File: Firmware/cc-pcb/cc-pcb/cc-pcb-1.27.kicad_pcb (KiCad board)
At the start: 2 copper layers, 39.4 x 36.8 mm, 19 parts, among them CON1 BARREL_JACK, IC1 ATMEGA328P-A, P1 CONN_20, P4 CONN_2, P5 CONN_6, P6 CONN_6, SW1 SRS

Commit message: cleaning up
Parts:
- CON1: value BARREL_JACK -> (none)
- D1, D2, D3, D4, D5, D6: value DIODE -> (none)
- IC1: value ATMEGA328P-A -> (none)
- P1: value CONN_20 -> (none)
- P4: value CONN_2 -> (none)
- P5, P6: value CONN_6 -> (none)
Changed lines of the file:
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@@
     (visible_elements 7FFFFBFF)
     (pcbplotparams
-      (layerselection 3178497)
+      (layerselection 284196865)
       (usegerberextensions true)
       (excludeedgelayer true)
@@
       (outputformat 1)
       (mirror false)
-      (drillshape 1)
+      (drillshape 0)
       (scaleselection 1)
-      (outputdirectory ""))
+      (outputdirectory D:/Tests/workspace/4DMC-Model/Firmware/cc-pcb/cc-pcb/))
   )
   (net 0 "")
@@
       (effects (font (size 1.016 1.016) (thickness 0.2032)))
     )
-    (fp_text value CONN_6 (at 0 3.81 180) (layer F.SilkS) hide
+    (fp_text value "" (at 0 3.81 180) (layer F.SilkS) hide
       (effects (font (size 1.016 1.016) (thickness 0.2032)))
     )
@@
       (effects (font (size 1.016 1.016) (thickness 0.2032)))
     )
-    (fp_text value CONN_6 (at 0 2.159 270) (layer F.SilkS) hide
+    (fp_text value "" (at 0 2.159 270) (layer F.SilkS) hide
       (effects (font (size 1.016 0.889) (thickness 0.2032)))
     )
@@
     (at 189.992 75.184)
     (descr "Hole 2mm")
-    (fp_text reference H1 (at 0 -2.794) (layer F.SilkS)
+    (fp_text reference H1 (at 0 -2.794) (layer F.SilkS) hide
       (effects (font (size 1.524 1.524) (thickness 0.3048)))
     )
@@
     (at 189.992 106.172)
     (descr "Hole 2mm")
-    (fp_text reference H2 (at 0 -2.794) (layer F.SilkS)
+    (fp_text reference H2 (at 0 -2.794) (layer F.SilkS) hide
       (effects (font (size 1.524 1.524) (thickness 0.3048)))
     )
@@
     (at 156.972 106.172)
     (descr "Hole 2mm")
-    (fp_text reference H3 (at 0 -2.794) (layer F.SilkS)
+    (fp_text reference H3 (at 0 -2.794) (layer F.SilkS) hide
       (effects (font (size 1.524 1.524) (thickness 0.3048)))
     )
@@
       (effects (font (size 1 1) (thickness 0.15)))
     )
-    (fp_text value CONN_20 (at 0 -3.8 90) (layer F.SilkS) hide
+    (fp_text value "" (at 0 -3.8 90) (layer F.SilkS) hide
       (effects (font (size 1 1) (thickness 0.15)))
     )
@@
   (module TQFP32 (layer F.Cu)
     (at 168.402 92.456 270)
-    (fp_text reference IC1 (at 0 -1.27 270) (layer F.SilkS)
+    (fp_text reference IC1 (at 0 0 270) (layer F.SilkS)
       (effects (font (size 1.27 1.016) (thickness 0.2032)))
     )
-    (fp_text value ATMEGA328P-A (at 0 1.905 270) (layer F.SilkS)
+    (fp_text value "" (at 0 1.905 270) (layer F.SilkS)
       (effects (font (size 1.27 1.016) (thickness 0.2032)))
     )
@@
       (effects (font (size 0.39878 0.39878) (thickness 0.09906)))
     )
-    (fp_text value DIODE (at 0 1.19888 90) (layer F.SilkS) hide
+    (fp_text value "" (at 0 1.19888 90) (layer F.SilkS) hide
       (effects (font (size 0.39878 0.39878) (thickness 0.09906)))
     )
@@
       (effects (font (size 0.39878 0.39878) (thickness 0.09906)))
     )
-    (fp_text value DIODE (at 0 1.19888 90) (layer F.SilkS) hide
+    (fp_text value "" (at 0 1.19888 90) (layer F.SilkS) hide
       (effects (font (size 0.39878 0.39878) (thickness 0.09906)))
     )
@@
       (effects (font (size 0.39878 0.39878) (thickness 0.09906)))
     )
-    (fp_text value DIODE (at 0 1.19888 90) (layer F.SilkS) hide
+    (fp_text value "" (at 0 1.19888 90) (layer F.SilkS) hide
       (effects (font (size 0.39878 0.39878) (thickness 0.09906)))
     )
@@
       (effects (font (size 0.39878 0.39878) (thickness 0.09906)))
     )
-    (fp_text value DIODE (at 0 1.19888 180) (layer F.SilkS) hide
+    (fp_text value "" (at 0 1.19888 180) (layer F.SilkS) hide
       (effects (font (size 0.39878 0.39878) (thickness 0.09906)))
     )
@@
       (effects (font (size 0.39878 0.39878) (thickness 0.09906)))
     )
-    (fp_text value DIODE (at 0 1.19888 180) (layer F.SilkS) hide
+    (fp_text value "" (at 0 1.19888 180) (layer F.SilkS) hide
       (effects (font (size 0.39878 0.39878) (thickness 0.09906)))
     )
@@
       (effects (font (size 0.39878 0.39878) (thickness 0.09906)))
     )
-    (fp_text value DIODE (at 0 1.19888 180) (layer F.SilkS) hide
+    (fp_text value "" (at 0 1.19888 180) (layer F.SilkS) hide
       (effects (font (size 0.39878 0.39878) (thickness 0.09906)))
     )
@@
       (effects (font (size 1.016 1.016) (thickness 0.2032)))
     )
-    (fp_text value CONN_2 (at 0.254 -3.556 90) (layer F.SilkS) hide
+    (fp_text value "" (at 0.254 -3.556 90) (layer F.SilkS) hide
       (effects (font (size 1.016 0.889) (thickness 0.2032)))
     )
@@
     (descr "DC Barrel Jack")
     (tags "Power Jack")
-    (fp_text reference CON1 (at 10.09904 0 90) (layer F.SilkS)
+    (fp_text reference CON1 (at 10.09904 0 90) (layer F.SilkS) hide
       (effects (font (size 1.016 1.016) (thickness 0.2032)))
     )
-    (fp_text value BARREL_JACK (at 0 -5.99948) (layer F.SilkS) hide
+    (fp_text value "" (at 0 -5.99948) (layer F.SilkS) hide
       (effects (font (size 1.016 1.016) (thickness 0.2032)))
     )
@@
   (segment (start 167.894002 83.438998) (end 175.178302 83.438998) (width 0.254) (layer F.Cu) (net 30))
   (segment (start 163.6268 87.7062) (end 167.894002 83.438998) (width 0.254) (layer F.Cu) (net 30))
-  (segment (start 157.48 94.996) (end 156.464 94.996) (width 1.016) (layer B.Cu) (net 31) (status 400000))
+  (segment (start 157.48 94.996) (end 156.464 94.996) (width 1.016) (layer B.Cu) (net 31))
   (segment (start 156.464 94.996) (end 155.575 94.107) (width 1.016) (layer B.Cu) (net 31))
   (segment (start 155.575 94.107) (end 155.575 85.471) (width 1.016) (layer B.Cu) (net 31))
@@
     (polygon
       (pts
-        (xy 191.008 95.25) (xy 187.198 99.187) (xy 187.198 109.22) (xy 159.766 109.22) (xy 159.766 103.378)
+        (xy 191.008 95.377) (xy 187.198 99.187) (xy 187.198 109.093) (xy 159.766 109.22) (xy 159.766 103.378)
         (xy 153.67 103.378) (xy 153.67 72.39) (xy 187.198 72.39) (xy 187.198 77.851) (xy 191.008 81.661)
       )
@@
     (polygon
       (pts
-        (xy 191.008 92.583) (xy 187.198 96.393) (xy 187.198 109.22) (xy 159.766 109.22) (xy 159.766 103.378)
+        (xy 191.008 95.377) (xy 187.198 99.187) (xy 187.198 109.22) (xy 159.766 109.22) (xy 159.766 103.378)
         (xy 153.67 103.378) (xy 153.67 72.39) (xy 187.198 72.39) (xy 187.198 77.851) (xy 191.008 81.661)
       )
     )
+  )
+  (zone (net 0) (net_name "") (layer F.Cu) (hatch edge 0.508)
+    (connect_pads (clearance 0.508))
+    (min_thickness 0.254)
+    (keepout (tracks allowed) (vias allowed) (copperpour not_allowed))
+    (fill (arc_segments 16) (thermal_gap 0.508) (thermal_bridge_width 0.508))
+    (polygon
+      (pts
+        (xy 171.831 95.758) (xy 164.973 95.758) (xy 164.973 89.027) (xy 171.831 89.027)
+      )
+    )
+  )
+  (zone (net 0) (net_name "") (layer F.Cu) (hatch edge 0.508)
+    (connect_pads (clearance 0.508))
+    (min_thickness 0.254)
+    (keepout (tracks allowed) (vias allowed) (copperpour not_allowed))
+    (fill (arc_segments 16) (thermal_gap 0.508) (thermal_bridge_width 0.508))
+    (polygon
+      (pts
+        (xy 168.021 84.582) (xy 171.196 84.582) (xy 171.196 84.963) (xy 170.18 85.979) (xy 169.291 85.979)
+        (xy 168.529 85.344) (xy 167.259 85.344) (xy 168.021 84.582)
+      )
+    )

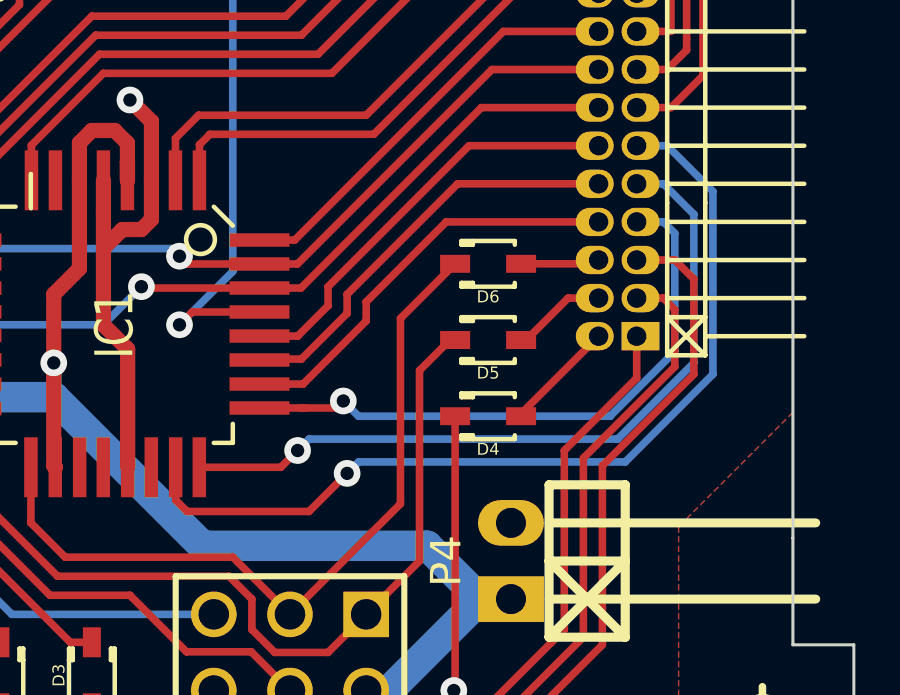
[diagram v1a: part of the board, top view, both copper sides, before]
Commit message: Increased GND width for LEDs
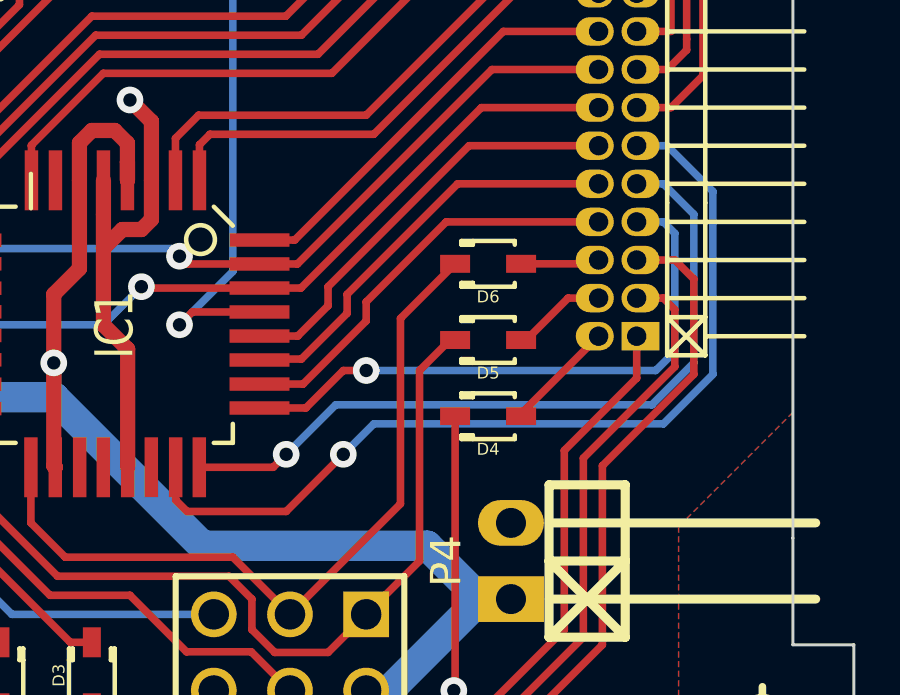
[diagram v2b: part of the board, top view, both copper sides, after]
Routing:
- net N-0000022: track 20.6 -> 20.0 mm
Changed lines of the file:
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@@
-(kicad_pcb (version 3) (host pcbnew "(2013-07-07 BZR 4022)-stable")
+(kicad_pcb (version 3) (host pcbnew "(2014-01-10 BZR 4027)-stable")
   (general
     (links 56)
@@
     (thickness 1.6)
     (drawings 9)
-    (tracks 309)
+    (tracks 306)
     (zones 0)
     (modules 19)
@@
     (19 F.Paste user)
     (20 B.SilkS user)
-    (21 F.SilkS user)
+    (21 F.SilkS user hide)
     (22 B.Mask user)
     (23 F.Mask user)
@@
   (segment (start 179.451 89.027) (end 176.784 91.694) (width 0.254) (layer F.Cu) (net 15))
   (segment (start 184.454326 89.103674) (end 184.531 89.027) (width 0.254) (layer F.Cu) (net 15))
-  (segment (start 184.912 95.504) (end 187.071 93.345) (width 0.254) (layer B.Cu) (net 16))
+  (segment (start 173.228 95.22968) (end 174.77232 95.22968) (width 0.254) (layer F.Cu) (net 16))
+  (segment (start 187.071 93.345) (end 187.071 89.408) (width 0.254) (layer B.Cu) (net 16))
+  (segment (start 187.071 89.408) (end 186.69 89.027) (width 0.254) (layer B.Cu) (net 16))
   (segment (start 186.69 89.027) (end 185.801 89.027) (width 0.254) (layer B.Cu) (net 16))
-  (segment (start 187.071 89.408) (end 186.69 89.027) (width 0.254) (layer B.Cu) (net 16))
-  (segment (start 187.071 93.345) (end 187.071 89.408) (width 0.254) (layer B.Cu) (net 16))
-  (segment (start 176.53 95.504) (end 184.912 95.504) (width 0.254) (layer B.Cu) (net 16))
-  (segment (start 184.912 95.504) (end 184.9254 95.504) (width 0.254) (layer B.Cu) (net 16))
-  (segment (start 174.625 95.2297) (end 175.7883 95.2297) (width 0.254) (layer F.Cu) (net 16))
-  (segment (start 176.022 94.996) (end 176.53 95.504) (width 0.254) (layer B.Cu) (net 16))
-  (via (at 176.022 94.996) (size 0.889) (layers F.Cu B.Cu) (net 16))
-  (segment (start 175.7883 95.2297) (end 176.022 94.996) (width 0.254) (layer F.Cu) (net 16))
-  (segment (start 173.228 95.2297) (end 174.625 95.2297) (width 0.254) (layer F.Cu) (net 16))
-  (segment (start 174.625 95.2297) (end 174.7547 95.2297) (width 0.254) (layer F.Cu) (net 16))
+  (segment (start 186.436 93.98) (end 187.071 93.345) (width 0.254) (layer B.Cu) (net 16))
+  (segment (start 176.784 93.98) (end 186.436 93.98) (width 0.254) (layer B.Cu) (net 16))
+  (via (at 176.784 93.98) (size 0.889) (layers F.Cu B.Cu) (net 16))
+  (segment (start 176.022 93.98) (end 176.784 93.98) (width 0.254) (layer F.Cu) (net 16))
+  (segment (start 174.77232 95.22968) (end 176.022 93.98) (width 0.254) (layer F.Cu) (net 16))
   (segment (start 181.94782 92.964) (end 182.118 92.964) (width 0.254) (layer F.Cu) (net 17))
   (segment (start 183.515 91.567) (end 184.531 91.567) (width 0.254) (layer F.Cu) (net 17))
@@
   (segment (start 175.514 91.186) (end 175.514 91.821) (width 0.254) (layer F.Cu) (net 19))
   (segment (start 180.213 86.487) (end 175.514 91.186) (width 0.254) (layer F.Cu) (net 19))
-  (segment (start 187.706 93.726) (end 185.166 96.266) (width 0.254) (layer B.Cu) (net 20))
-  (via (at 174.498 96.647) (size 0.889) (layers F.Cu B.Cu) (net 20))
-  (segment (start 174.498 96.647) (end 173.9392 97.2058) (width 0.254) (layer F.Cu) (net 20))
-  (segment (start 171.2214 97.2058) (end 173.9392 97.2058) (width 0.254) (layer F.Cu) (net 20))
+  (segment (start 173.6852 97.2058) (end 174.117 96.774) (width 0.254) (layer F.Cu) (net 20))
+  (segment (start 185.801 87.757) (end 186.69 87.757) (width 0.254) (layer B.Cu) (net 20))
+  (segment (start 187.706 88.773) (end 187.706 93.726) (width 0.254) (layer B.Cu) (net 20))
   (segment (start 186.69 87.757) (end 187.706 88.773) (width 0.254) (layer B.Cu) (net 20))
-  (segment (start 187.706 88.773) (end 187.706 93.726) (width 0.254) (layer B.Cu) (net 20))
-  (segment (start 186.69 87.757) (end 185.801 87.757) (width 0.254) (layer B.Cu) (net 20))
-  (segment (start 174.879 96.266) (end 174.498 96.647) (width 0.254) (layer B.Cu) (net 20))
-  (segment (start 185.166 96.266) (end 174.879 96.266) (width 0.254) (layer B.Cu) (net 20))
+  (segment (start 186.309 95.123) (end 187.706 93.726) (width 0.254) (layer B.Cu) (net 20))
+  (segment (start 175.768 95.123) (end 186.309 95.123) (width 0.254) (layer B.Cu) (net 20))
+  (segment (start 173.6852 97.2058) (end 171.2214 97.2058) (width 0.254) (layer F.Cu) (net 20))
+  (segment (start 174.117 96.774) (end 175.768 95.123) (width 0.254) (layer B.Cu) (net 20))
+  (via (at 174.117 96.774) (size 0.889) (layers F.Cu B.Cu) (net 20))
+  (segment (start 174.117 98.679) (end 176.022 96.774) (width 0.254) (layer F.Cu) (net 21))
+  (segment (start 170.434 98.298) (end 170.815 98.679) (width 0.254) (layer F.Cu) (net 21))
+  (segment (start 170.815 98.679) (end 174.117 98.679) (width 0.254) (layer F.Cu) (net 21))
+  (segment (start 177.038 95.758) (end 186.69 95.758) (width 0.254) (layer B.Cu) (net 21))
+  (segment (start 186.69 95.758) (end 188.341 94.107) (width 0.254) (layer B.Cu) (net 21))
   (segment (start 185.801 86.487) (end 186.817 86.487) (width 0.254) (layer B.Cu) (net 21))
-  (segment (start 170.434 98.298) (end 170.434 97.2058) (width 0.254) (layer F.Cu) (net 21))
-  (via (at 176.149 97.409) (size 0.889) (layers F.Cu B.Cu) (net 21))
-  (segment (start 174.879 98.679) (end 176.149 97.409) (width 0.254) (layer F.Cu) (net 21))
-  (segment (start 170.815 98.679) (end 174.879 98.679) (width 0.254) (layer F.Cu) (net 21))
-  (segment (start 170.434 98.298) (end 170.815 98.679) (width 0.254) (layer F.Cu) (net 21))
-  (segment (start 176.53 97.028) (end 176.149 97.409) (width 0.254) (layer B.Cu) (net 21))
-  (segment (start 185.42 97.028) (end 176.53 97.028) (width 0.254) (layer B.Cu) (net 21))
-  (segment (start 188.341 94.107) (end 185.42 97.028) (width 0.254) (layer B.Cu) (net 21))
   (segment (start 188.341 88.011) (end 188.341 94.107) (width 0.254) (layer B.Cu) (net 21))
   (segment (start 186.817 86.487) (end 188.341 88.011) (width 0.254) (layer B.Cu) (net 21))
+  (segment (start 170.434 98.298) (end 170.434 97.2058) (width 0.254) (layer F.Cu) (net 21))
+  (segment (start 176.022 96.774) (end 177.038 95.758) (width 0.254) (layer B.Cu) (net 21))
+  (via (at 176.022 96.774) (size 0.889) (layers F.Cu B.Cu) (net 21))
   (segment (start 181.94782 90.424) (end 184.404 90.424) (width 0.254) (layer F.Cu) (net 22))
   (segment (start 184.404 90.424) (end 184.531 90.297) (width 0.254) (layer F.Cu) (net 22))
@@
       )
     )
+  )
+  (zone (net 0) (net_name "") (layer F.Cu) (hatch edge 0.508)
+    (connect_pads (clearance 0.508))
+    (min_thickness 0.254)
+    (keepout (tracks allowed) (vias allowed) (copperpour not_allowed))
+    (fill (arc_segments 16) (thermal_gap 0.508) (thermal_bridge_width 0.508))
+    (polygon
+      (pts
+        (xy 183.007 98.171) (xy 180.086 98.171) (xy 180.086 96.52) (xy 183.007 96.52)
+      )
+    )
+  )
+  (zone (net 0) (net_name "") (layer F.Cu) (hatch edge 0.508)
+    (connect_pads (clearance 0.508))
+    (min_thickness 0.254)
+    (keepout (tracks allowed) (vias allowed) (copperpour not_allowed))
+    (fill (arc_segments 16) (thermal_gap 0.508) (thermal_bridge_width 0.508))
+    (polygon
+      (pts
+        (xy 171.45 77.978) (xy 170.688 77.978) (xy 169.926 76.835) (xy 169.672 76.835) (xy 169.672 74.168)
+        (xy 169.545 74.168) (xy 169.545 73.914) (xy 171.069 73.914) (xy 171.069 74.168) (xy 170.561 74.168)
+        (xy 170.561 76.835) (xy 171.45 76.835) (xy 171.45 77.978)
+      )
+    )

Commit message: Moved 2x10 pin, changed it a bit
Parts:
- CON1: value (none) -> BARREL_JACK
- D1, D2, D3, D4, D5, D6: value (none) -> DIODE
- IC1: value (none) -> ATMEGA328P-A
- P1: value (none) -> CONN_20; footprint pin_strip_1.27mm_10x2_90 -> pin_strip_1.27mm_10x2_90b
- P4: value (none) -> CONN_2
- P5, P6: value (none) -> CONN_6
- moved P1 1.63 mm to (183.9, 88.1)
- moved D4 1.26 mm to (180.0, 96.4)
- moved D5 1.26 mm to (180.0, 93.9)
- moved D6 1.26 mm to (180.0, 91.3)
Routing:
- net GND: track 19.1 -> 55.2 mm
- net N-0000021: track 14.0 -> 12.2 mm
- net N-0000022: track 20.0 -> 18.3 mm
- net N-0000028: track 30.3 -> 28.6 mm
- net N-0000026: track 14.3 -> 12.6 mm
- net N-0000011: track 16.6 -> 14.9 mm
- net N-000004: track 29.9 -> 28.3 mm
- net N-000002: track 14.2 -> 12.5 mm
- net N-0000020: track 14.2 -> 12.5 mm
- net N-000003: track 30.1 -> 28.4 mm
- net N-0000018: track 41.4 -> 39.8 mm
- net N-0000010: track 19.9 -> 18.3 mm
- net N-0000019: track 28.4 -> 26.8 mm
- net N-0000017: track 35.3 -> 33.8 mm
- net N-0000027: track 25.2 -> 23.7 mm
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
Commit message: in the middle of routing...
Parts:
- added P10: CONN_1, PINTST, F.Cu at (113.3, 128.0)
- added P11: CONN_1, PINTST, F.Cu at (107.7, 128.0)
- added P2: CONN_2, XH2.54_2-90, F.Cu at (124.3, 109.0)
- added P7: CONN_1, PINTST, F.Cu at (121.3, 120.0)
- added P8: CONN_1, PINTST, F.Cu at (102.4, 114.3)
- added P9: CONN_1, PINTST, F.Cu at (105.9, 125.7)
- C1, C2, D4, D5, D6, R1: moved to B.Cu
- P4: value CONN_2 -> CONN_1; footprint pin_strip_2-90 -> PINTST
- P5: value CONN_6 -> CONN_1; footprint PIN_ARRAY-6X1 -> PINTST
- P6: value CONN_6 -> CONN_1; footprint pin_array_3x2 -> PINTST
- moved D4 77.0 mm to (110.6, 129.9)
- moved D5 72.8 mm to (116.5, 129.5)
- moved C2 71.8 mm to (106.4, 116.8)
- moved C1 71.0 mm to (110.0, 113.0), turned to 180 degrees
- moved D6 70.2 mm to (119.8, 127.5)
- moved R1 69.4 mm to (111.8, 116.8)
- moved SW1 69.1 mm to (117.6, 108.2), turned to 90 degrees
- moved P1 68.4 mm to (124.5, 121.9)
- moved H2 67.0 mm to (129.0, 133.9)
- moved H1 66.8 mm to (129.0, 102.6)
- moved IC1 63.2 mm to (111.8, 120.5)
- moved D1 61.1 mm to (102.9, 121.2)
- moved H3 60.3 mm to (103.4, 133.9)
- moved CON1 60.3 mm to (103.9, 104.6)
- moved P5 57.8 mm to (102.4, 111.3)
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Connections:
- C2 pad 1: N-0000015 (its old number) -> N-0000011
- D4 pad 1: N-0000024 (its old number) -> N-0000019
- D4 pad 2: N-0000012 (its old number) -> N-000008
- D5 pad 1: N-0000023 -> N-0000018
- D5 pad 2: N-0000014 (its old number) -> N-0000010
- D6 pad 1: N-0000029 -> N-0000020
- D6 pad 2: N-0000013 (its old number) -> N-000009
- IC1 pad 15: N-0000012 (its old number) -> N-000008
- IC1 pad 16: N-0000014 (its old number) -> N-0000010
- IC1 pad 17: N-0000013 (its old number) -> N-000009
- IC1 pad 23: N-0000028 -> N-0000023
- IC1 pad 24: N-0000027 (its old number) -> N-0000022
- IC1 pad 25: N-0000022 -> N-0000021
- IC1 pad 29: N-0000015 (its old number) -> N-0000011
- IC1 pad 30: N-000003 -> N-000007
- IC1 pad 31: N-000004 (its old number) -> N-000003
- P1 pad 11: N-0000028 -> N-0000019
- P1 pad 14: N-000003 -> N-000007
- P1 pad 16: N-000004 (its old number) -> N-000003
- P1 pad 2: N-0000024 (its old number) -> N-0000023
- P1 pad 4: N-0000023 -> N-0000022
- P1 pad 6: N-0000029 -> N-0000021
- P1 pad 7: N-0000022 -> N-0000020
- P1 pad 9: N-0000027 (its old number) -> N-0000018
- P4 pad 1: VCC -> GND
- P6 pad 1: N-0000014 (its old number) -> N-000003
- R1 pad 2: N-0000015 (its old number) -> N-0000011
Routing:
- net VCC: track 86.8 -> 15.4 mm
- net N-0000015 (its old number): track 56.1 -> 0.00 mm, vias 3 -> 0
- net GND: track 55.2 -> 14.4 mm, vias 1 -> 0
- net N-0000012 (its old number): track 34.6 -> 0.00 mm, vias 1 -> 0
- net N-0000030: track 33.7 -> 0.00 mm
- net N-0000033: track 44.4 -> 11.3 mm
- net N-000004: track 30.2 -> 0.00 mm
- net N-0000031: track 39.6 -> 9.36 mm
- net N-0000028: track 28.6 -> 0.00 mm, vias 1 -> 0
- net N-0000014 (its old number): track 28.4 -> 0.00 mm
- net N-000004 (its old number): track 28.3 -> 0.00 mm, vias 1 -> 0
- net N-0000013 (its old number): track 24.5 -> 0.00 mm
- net N-0000019: track 0.00 -> 24.2 mm
- net N-0000027 (its old number): track 23.7 -> 0.00 mm, vias 1 -> 0
- net N-0000014: track 33.8 -> 12.0 mm
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- removed copper zone on B.Cu, net GND
- removed copper zone on F.Cu, net GND
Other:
- board size 39.4 x 36.8 mm -> 31.5 x 36.8 mm
- net class PWR: trace_width 1.016 -> 2.032

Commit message: in the middle of something...
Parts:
- moved P11 2.16 mm to (109.9, 127.9)
- moved P6 2.16 mm to (121.5, 118.4)
- moved P8 2.16 mm to (104.5, 114.2)
- moved P9 2.16 mm to (108.1, 125.6)
- moved D1 2.16 mm to (105.0, 121.0)
- moved D3 2.16 mm to (121.3, 127.4)
- moved IC1 2.16 mm to (113.9, 120.4)
- moved P10 2.16 mm to (115.4, 127.9)
- moved D2 2.16 mm to (119.0, 129.4)
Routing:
- net (no net): track 0.00 -> 24.4 mm
- net N-0000015: track 36.4 -> 17.4 mm
- net N-0000019: track 24.2 -> 11.6 mm
- net N-0000023: track 11.7 -> 2.26 mm
- net N-0000027: track 13.9 -> 4.72 mm
- net N-0000018: track 17.4 -> 8.75 mm
- net N-000009: track 11.9 -> 3.99 mm
- net N-0000024: track 21.3 -> 14.2 mm
- net N-0000025: track 21.9 -> 15.3 mm
- net N-000003: track 7.35 -> 1.64 mm
- net N-000002: track 7.65 -> 2.16 mm
- net N-0000022: track 9.70 -> 4.36 mm
- net N-000007: track 7.54 -> 2.33 mm
- net N-000005: track 7.40 -> 2.95 mm
- net N-0000016: track 7.59 -> 3.28 mm
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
